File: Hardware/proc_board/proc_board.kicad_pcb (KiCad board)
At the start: 2 copper layers, 80.8 x 60.1 mm, 18 parts, among them J1 Conn_01x40, U1 74HC21, U2 W65C02SxP, U3 HM62256BLP, U4 28C256, U5 74HC00, U6 HM62256BLP

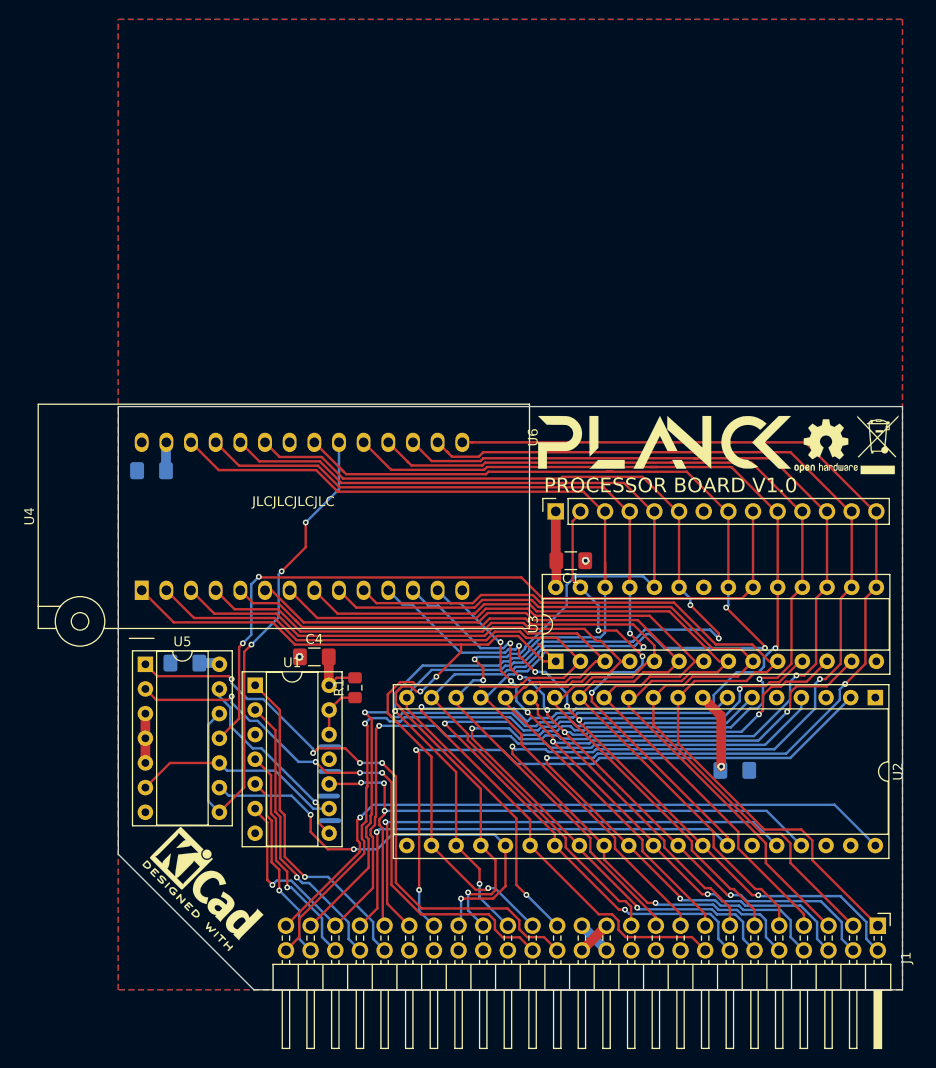
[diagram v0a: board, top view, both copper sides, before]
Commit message: rounded corners
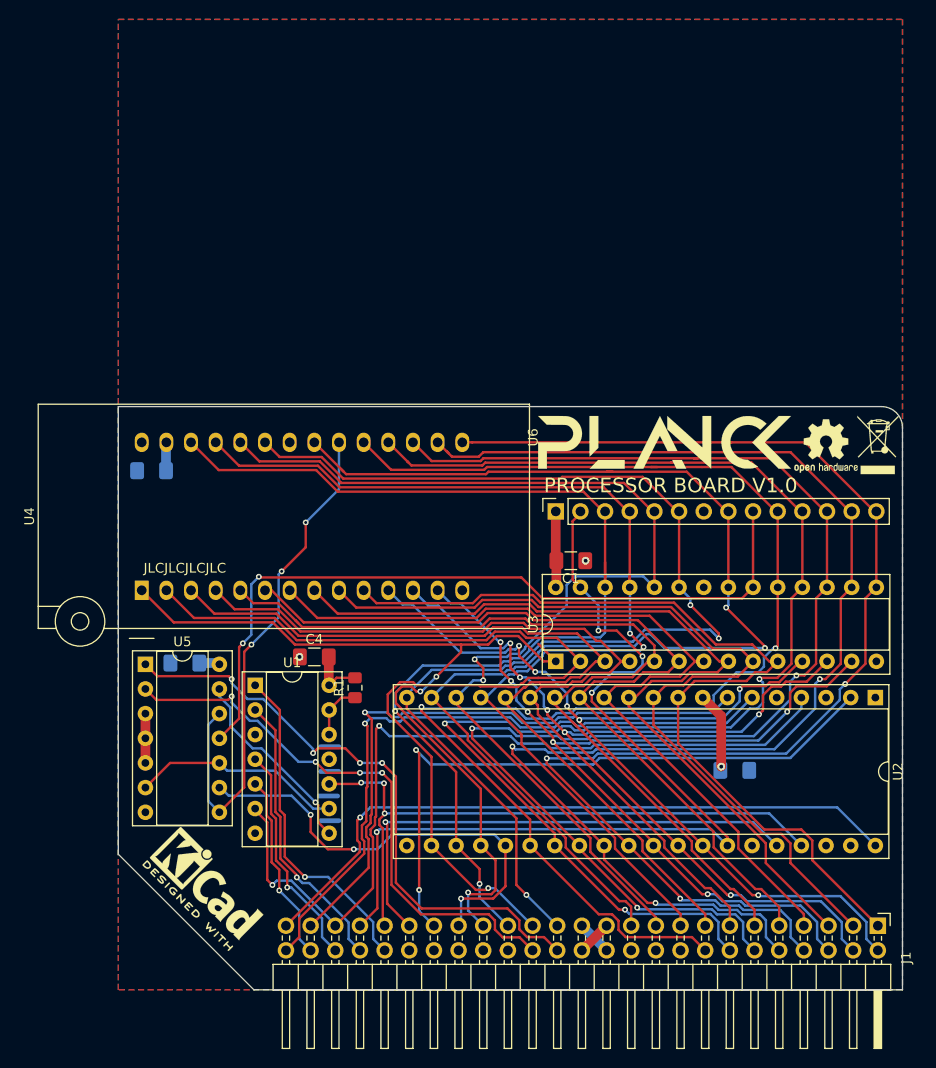
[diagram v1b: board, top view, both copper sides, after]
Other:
- outline, holes or cut-outs redrawn
